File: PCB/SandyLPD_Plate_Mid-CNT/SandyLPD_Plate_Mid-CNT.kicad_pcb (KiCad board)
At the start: 2 copper layers, 49.4 x 61 mm, 17 parts

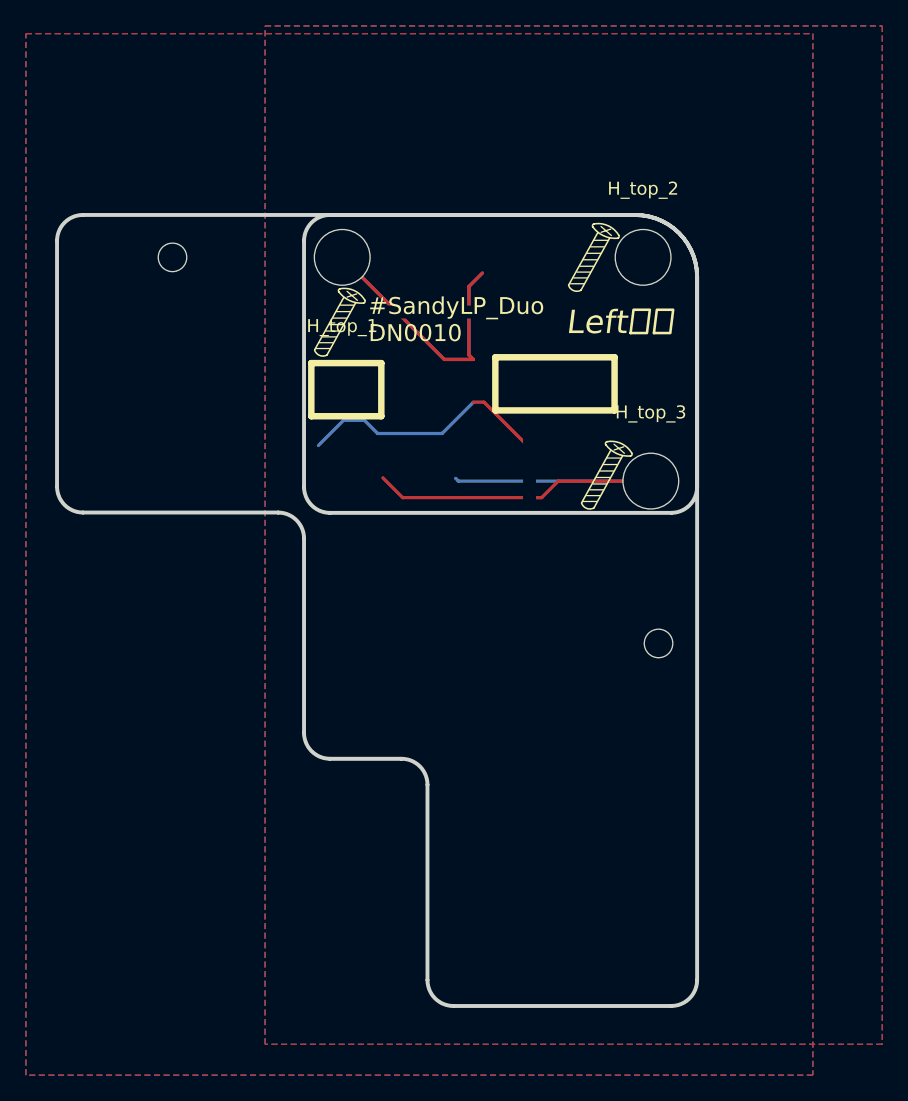
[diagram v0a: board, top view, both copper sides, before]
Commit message: Top基板裏側のソケットを逃す穴を作成
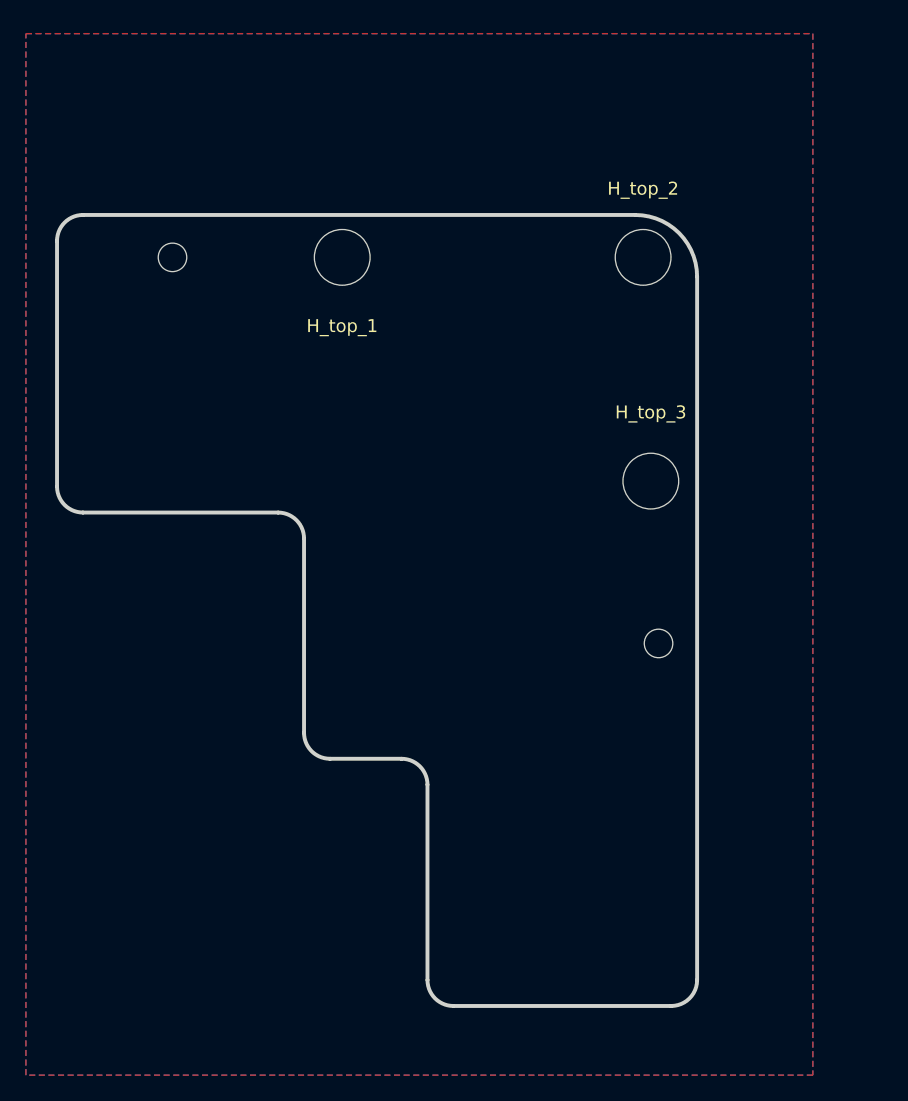
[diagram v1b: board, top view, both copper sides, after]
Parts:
- removed REF** (x6): ICON_Screw_Long_Medium, locallib:ICON_Screw_Long_Medium
- removed REF**: 60_Outline, locallib:SandyLPD_outline_Top
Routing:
- net (no net): track 97.9 -> 0.00 mm
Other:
- board text removed: "#SandyLP_Duo DN0010"
- board text removed: "Left 左"
- board text removed: "Right 右"

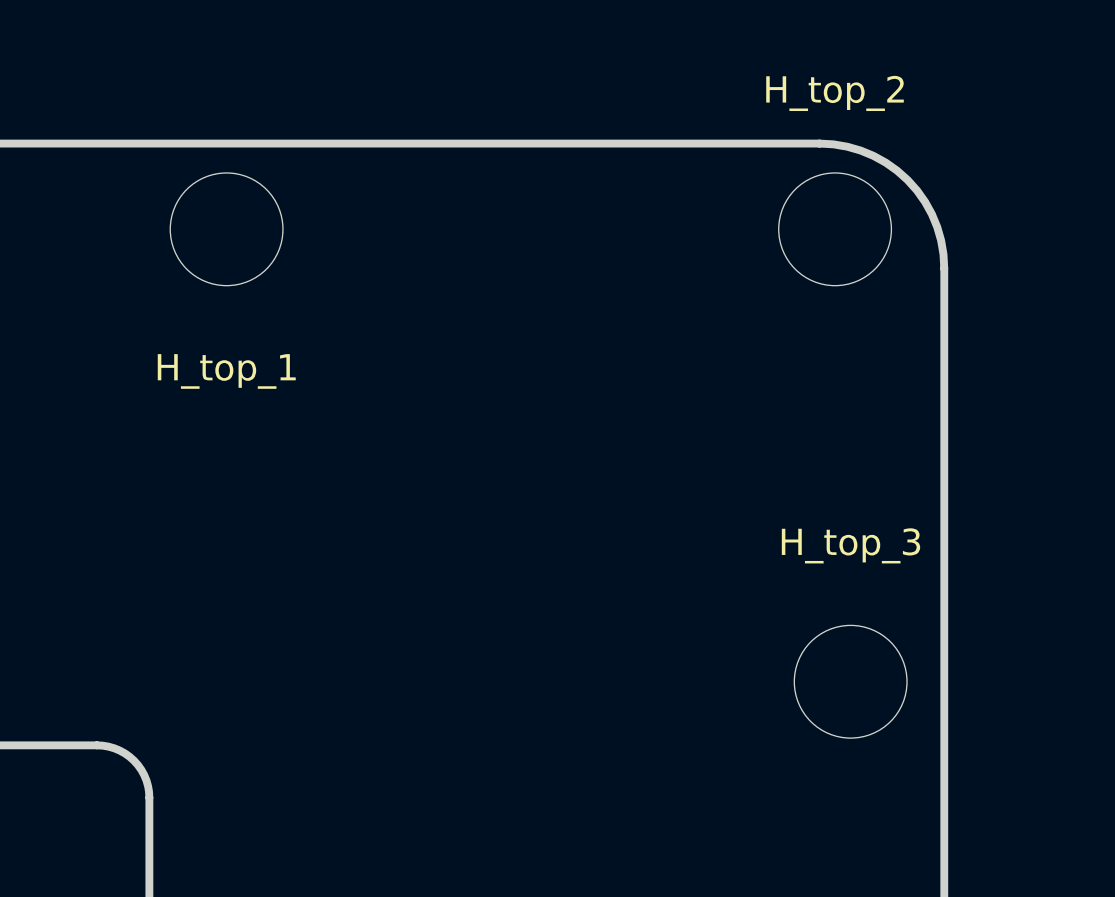
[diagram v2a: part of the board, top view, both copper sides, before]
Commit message: 基板Top裏側のパーツ逃し穴を調整
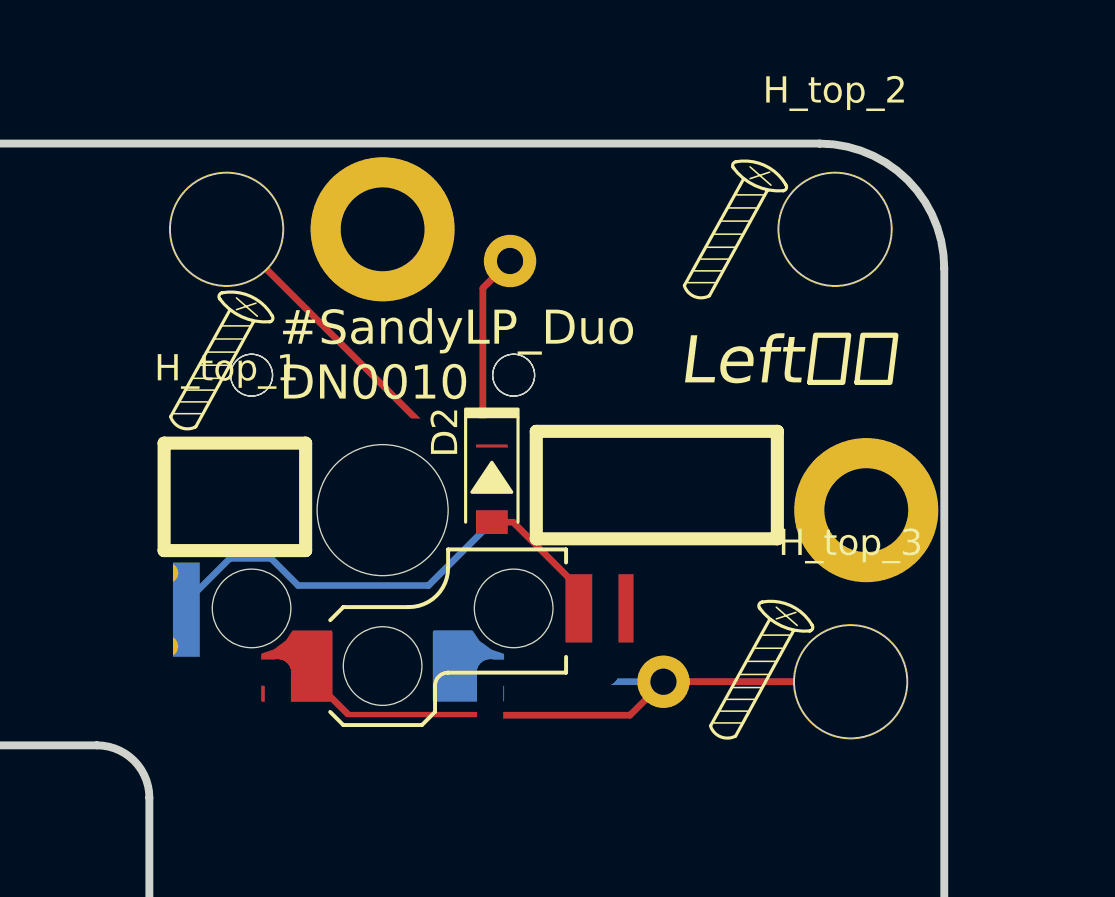
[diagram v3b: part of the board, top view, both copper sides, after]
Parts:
- added D1: D, locallib:D_SOD-123_Emphasized_Direction_Line, B.Cu at (139.5, 48.4)
- added D2: D, locallib:D_SOD-123_Emphasized_Direction_Line, F.Cu at (139.5, 48.4)
- added H1: MountingHole, locallib:MountingHole_2.2mm_M2_Pad_minimal, F.Cu at (129.4, 38.9)
- added H2: MountingHole, locallib:MountingHole_2.2mm_M2_Pad_minimal, F.Cu at (153.2, 56.2)
- added H3: MountingHole, locallib:MountingHole_M2_Through-hole_tap_THC-0.8-x-2, F.Cu at (135.4, 38.9)
- added H4: MountingHole, locallib:MountingHole_M2_Through-hole_tap_THC-0.8-x-2, F.Cu at (153.8, 49.6)
- added H5: MountingHole, locallib:MountingHole_2.2mm_M2_Pad_minimal, F.Cu at (152.6, 38.9)
- added REF**: ICON_Screw_Long_Medium, locallib:ICON_Screw_Long_Medium, F.Cu at (128.6, 47.5)
- added REF**: ICON_Screw_Long_Medium, locallib:ICON_Screw_Long_Medium, F.Cu at (149.2, 59.3)
- added REF**: ICON_Screw_Long_Medium, locallib:ICON_Screw_Long_Medium, F.Cu at (148.2, 42.5)
- added REF**: ICON_Screw_Long_Medium, locallib:ICON_Screw_Long_Medium, B.Cu at (150.1, 42.9)
- added REF**: ICON_Screw_Long_Medium, locallib:ICON_Screw_Long_Medium, B.Cu at (132.1, 47.1)
- added REF**: ICON_Screw_Long_Medium, locallib:ICON_Screw_Long_Medium, B.Cu at (150.1, 59.3)
- added SW_T1: SW_Push, locallib:Kailh_socket_ChocV2_for_Reverse, B.Cu at (135.4, 49.6)
- added SW_Y1: SW_Push, locallib:Kailh_socket_ChocV2_small_#2pad_for_Reverse_no_hole, F.Cu at (135.4, 49.6)
- added T_C5: Conn_01x01, locallib:TestPoint_THTPad_D2.0mm_Drill1.0mm, B.Cu at (146.1, 56.2)
- added T_R0: Conn_01x01, locallib:TestPoint_THTPad_D2.0mm_Drill1.0mm, B.Cu at (140.2, 40.1)
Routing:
- net (no net): track 0.00 -> 97.9 mm
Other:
- board text added: "#SandyLP_Duo DN0010"
- board text added: "Left 左"
- board text added: "Right 右"

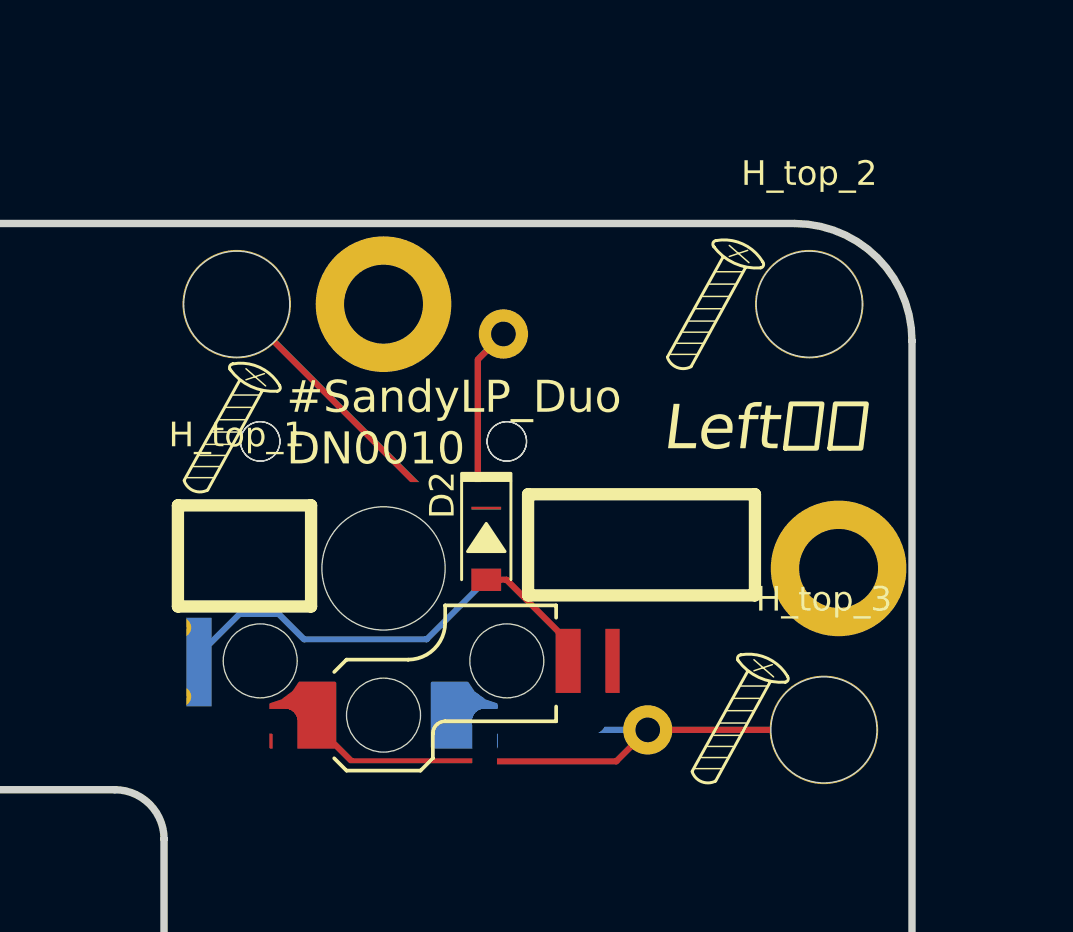
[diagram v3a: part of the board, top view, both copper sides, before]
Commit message: 不要部品削除
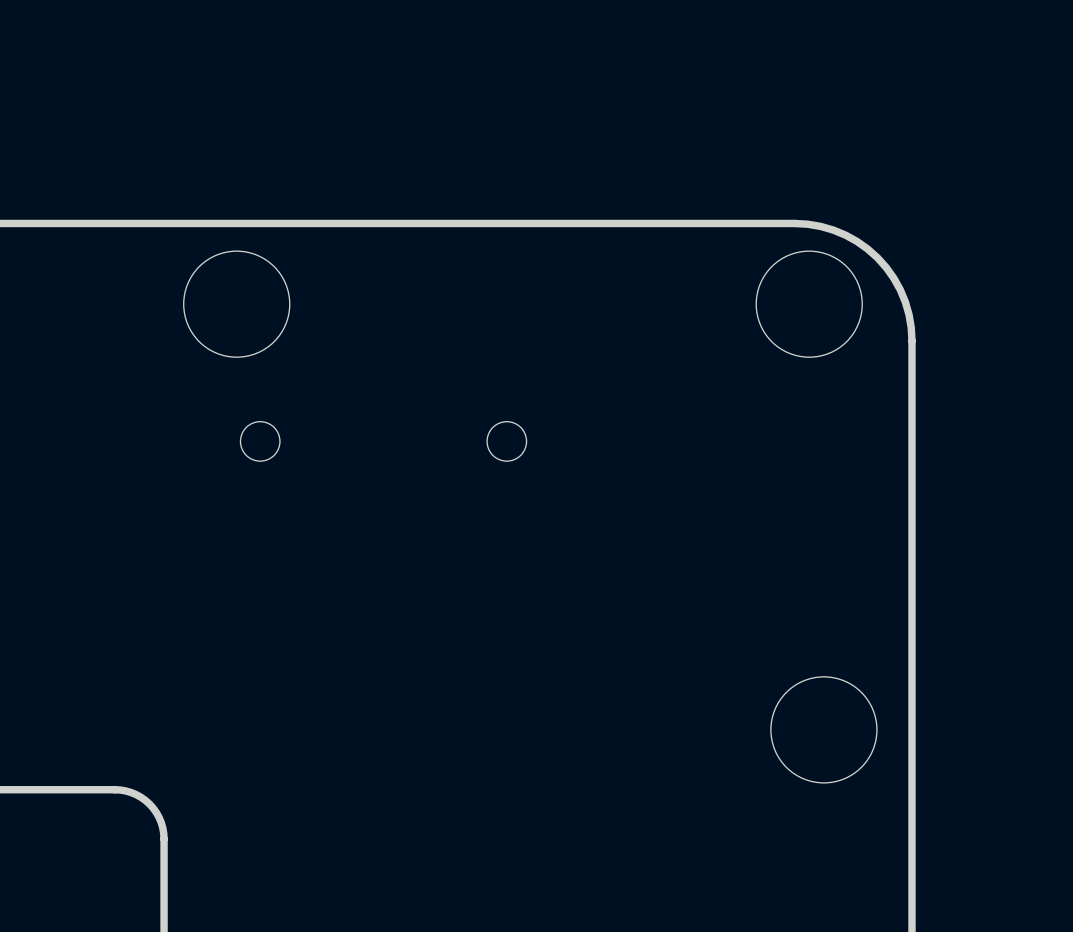
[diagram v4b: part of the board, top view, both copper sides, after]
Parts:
- removed D1, D2: D, locallib:D_SOD-123_Emphasized_Direction_Line
- removed H1, H2: MountingHole, locallib:MountingHole_2.2mm_M2_Pad_minimal
- removed H3, H4: MountingHole, locallib:MountingHole_M2_Through-hole_tap_THC-0.8-x-2
- removed the H5 at (152.6, 38.9)
- removed REF** (x6): ICON_Screw_Long_Medium, locallib:ICON_Screw_Long_Medium
- removed SW_T1: SW_Push, locallib:Kailh_socket_ChocV2_for_Reverse
- removed SW_Y1: SW_Push, locallib:Kailh_socket_ChocV2_small_#2pad_for_Reverse_no_hole
- removed T_C5, T_R0: Conn_01x01, locallib:TestPoint_THTPad_D2.0mm_Drill1.0mm
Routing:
- net (no net): track 97.9 -> 0.00 mm
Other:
- board text removed: "#SandyLP_Duo DN0010"
- board text removed: "Left 左"
- board text removed: "Right 右"
